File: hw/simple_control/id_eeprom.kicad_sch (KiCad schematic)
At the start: 6 parts, among them U3 CAT24C256

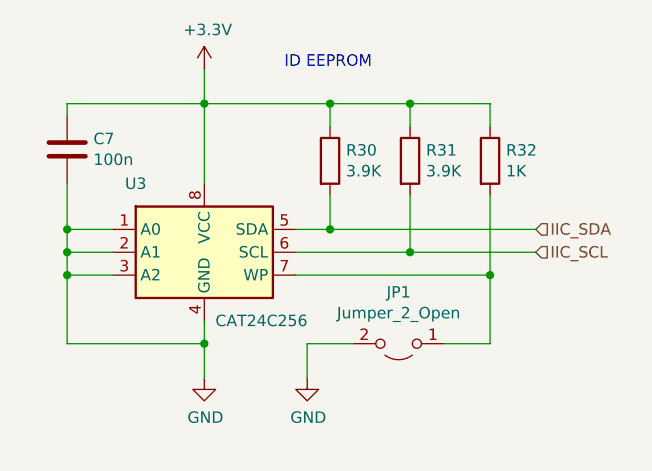
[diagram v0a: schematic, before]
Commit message: [hw] Add CPU modules
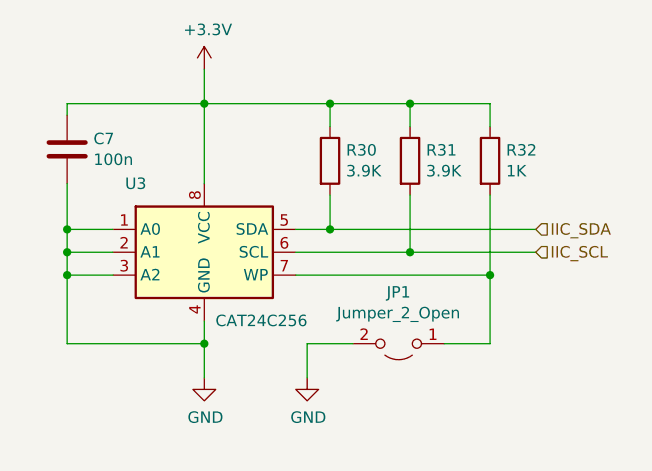
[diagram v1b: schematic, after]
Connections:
- net +3V3 renamed +3.3V
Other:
- note removed: "ID EEPROM"
- company: (none) -> Stefan Misik
- title: (none) -> WS2812 Simple Controller
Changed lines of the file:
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@@
 (kicad_sch (version 20230121) (generator eeschema)
   (paper "A4")
+  (title_block
+    (title "WS2812 Simple Controller")
+    (date "2023-03-09")
+    (company "Stefan Misik")
+    (comment 1 "ID EEPROM")
+  )
   (junction (at 137.795 99.06) (diameter 0) (color 0 0 0 0)
   )
@@
   (wire (pts (xy 137.795 85.09) (xy 123.825 85.09))
     (stroke (width 0) (type default))
-  )
-  (text "ID EEPROM" (at 132.715 81.28 0)
-    (effects (font (size 1.27 1.27)) (justify left bottom))
   )
   (hierarchical_label "IIC_SCL" (shape input) (at 160.655 101.6 0) (fields_autoplaced)
@@
     )
   )
-  (symbol (lib_name "GND_1") (lib_id "power:GND") (at 123.825 115.57 0) (unit 1)
+  (symbol (lib_id "power:GND") (at 123.825 115.57 0) (unit 1)
     (in_bom yes) (on_board yes) (dnp no)
     (property "Reference" "#PWR030" (at 123.825 121.92 0)

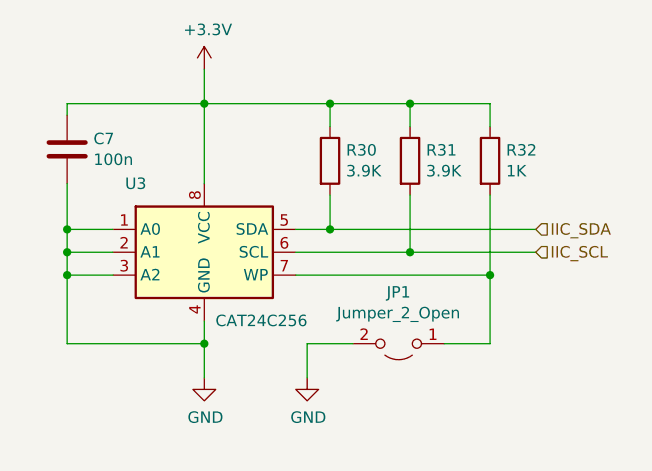
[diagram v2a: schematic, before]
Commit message: [hw] Fix ERC issues, update RPi Pico library
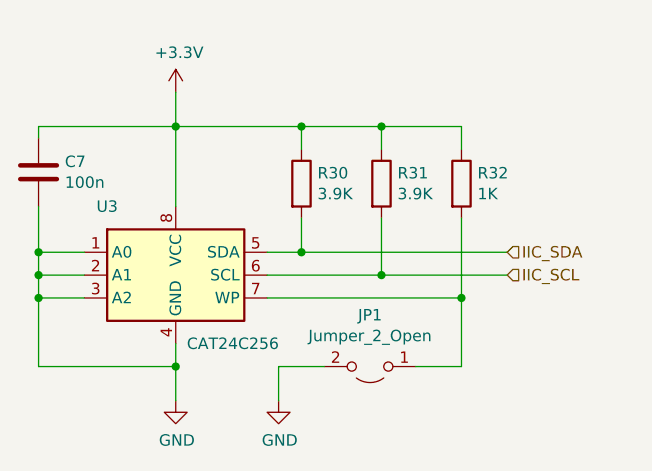
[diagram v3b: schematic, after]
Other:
- moved on the sheet: C7, JP1, R30, R31, R32, U3

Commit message: chore(hw): layout ID EEPROM
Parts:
- JP1: footprint Connector_PinHeader_2.54mm:PinHeader_1x02_P2.54mm_Horizontal -> Connector_PinHeader_2.54mm:PinHeader_1x02_P2.54mm_Vertical
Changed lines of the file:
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@@
       (effects (font (size 1.27 1.27)))
     )
-    (property "Footprint" "Connector_PinHeader_2.54mm:PinHeader_1x02_P2.54mm_Horizontal" (at 142.24 114.3 0)
+    (property "Footprint" "Connector_PinHeader_2.54mm:PinHeader_1x02_P2.54mm_Vertical" (at 142.24 114.3 0)
       (effects (font (size 1.27 1.27)) hide)
     )
